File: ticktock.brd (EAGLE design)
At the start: 61 x 67.3 mm, 64 parts, among them IC1 ATMEGA644A, IC2 AD8611R, IC3 REF200U, J1 AVR_SPI_PRG_6NS, Q1 MOSFET-NCHANNEL2N7002PW, Q2 MOSFET-NCHANNELBSS138, Q3 MOSFET-NCHANNELBSS138, U1 MAX232SOIC16, U2 OSCILLATORSMD, U3 FT232RLSSOP, U4 BMP180

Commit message: Preliminary Route completed.
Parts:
- moved ATC4 2.03 mm to (19.8, 19.6), turned to 0 degrees
- moved GPR2 0.57 mm to (21.3, 8.64)
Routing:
- net GPS_TX: track 0.00 -> 122.0 mm, vias 0 -> 2
- net GPS_RX: track 0.00 -> 81.7 mm
- net 3.3V: track 28.5 -> 81.2 mm, vias 2 -> 6
- net 5V: track 291.8 -> 294.4 mm

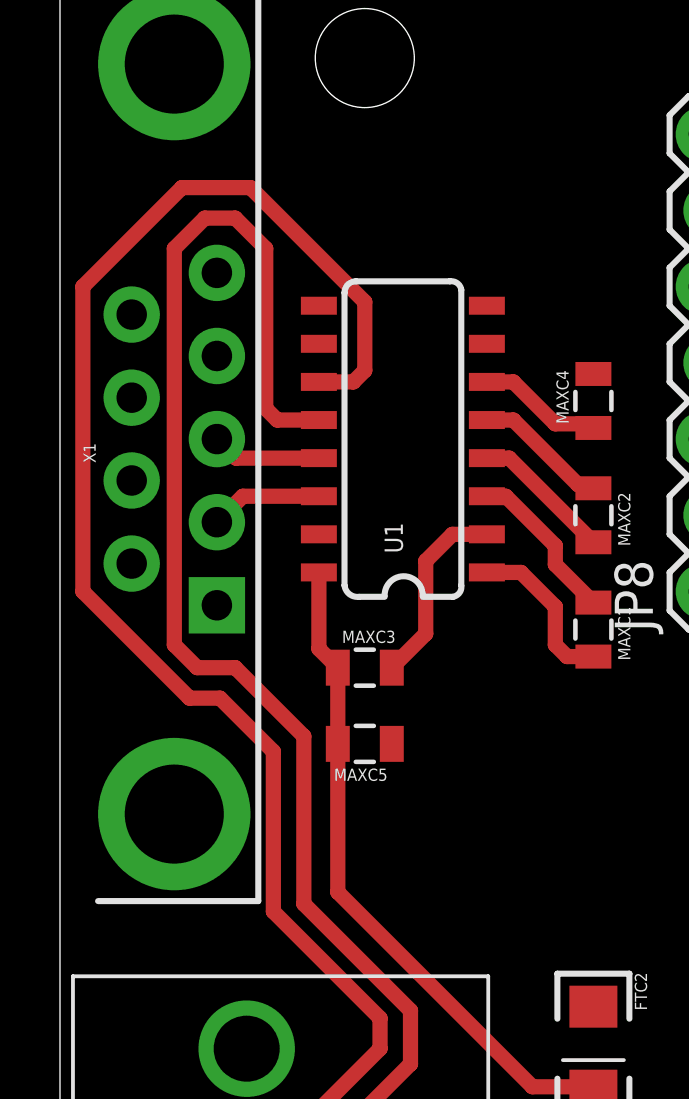
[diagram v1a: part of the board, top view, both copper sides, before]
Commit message: Fix traces around RS232 pins to use vias instead.
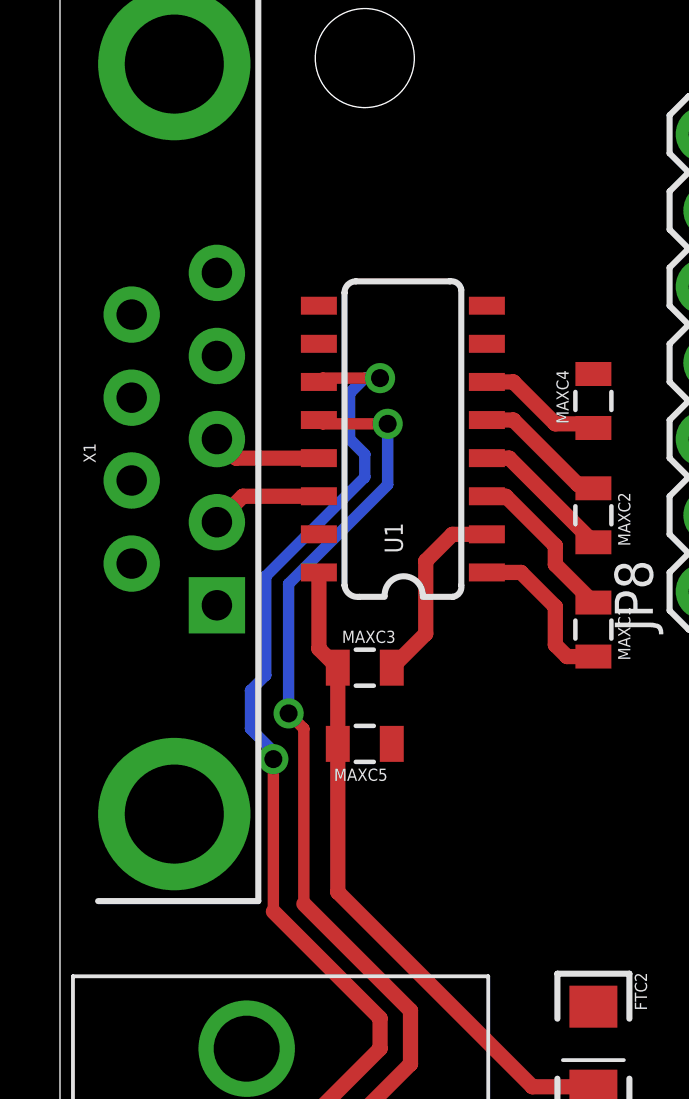
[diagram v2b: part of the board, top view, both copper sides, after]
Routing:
- net GPS_TX: track 122.0 -> 104.3 mm, vias 2 -> 4
- net GPS_RX: track 81.7 -> 66.1 mm, vias 0 -> 2
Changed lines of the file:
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@@
 <wire x1="33.824" y1="17.06" x2="33.02" y2="16.256" width="0.508" layer="1"/>
 <via x="33.02" y="16.256" extent="1-16" drill="0.6"/>
-<wire x1="8.63" y1="52.705" x2="9.779" y2="52.705" width="0.508" layer="1"/>
-<wire x1="9.779" y1="52.705" x2="10.16" y2="53.086" width="0.508" layer="1"/>
-<wire x1="10.16" y1="53.086" x2="10.16" y2="55.372" width="0.508" layer="1"/>
-<wire x1="10.16" y1="55.372" x2="6.35" y2="59.182" width="0.508" layer="1"/>
-<wire x1="6.35" y1="59.182" x2="4.064" y2="59.182" width="0.508" layer="1"/>
-<wire x1="4.064" y1="59.182" x2="0.762" y2="55.88" width="0.508" layer="1"/>
-<wire x1="0.762" y1="55.88" x2="0.762" y2="45.72" width="0.508" layer="1"/>
-<wire x1="0.762" y1="45.72" x2="4.318" y2="42.164" width="0.508" layer="1"/>
-<wire x1="4.318" y1="42.164" x2="5.334" y2="42.164" width="0.508" layer="1"/>
-<wire x1="5.334" y1="42.164" x2="7.112" y2="40.386" width="0.508" layer="1"/>
-<wire x1="7.112" y1="40.386" x2="7.112" y2="35.052" width="0.508" layer="1"/>
 <wire x1="7.112" y1="35.052" x2="10.668" y2="31.496" width="0.508" layer="1"/>
 <wire x1="10.668" y1="31.496" x2="10.668" y2="30.48" width="0.508" layer="1"/>
@@
 <wire x1="8.382" y1="10.16" x2="9.906" y2="11.684" width="0.381" layer="1"/>
 <wire x1="9.906" y1="11.684" x2="9.906" y2="20.066" width="0.381" layer="1"/>
+<wire x1="7.112" y1="35.052" x2="7.112" y2="40.132" width="0.381" layer="1"/>
+<via x="7.112" y="40.132" extent="1-16" drill="0.6"/>
+<wire x1="7.112" y1="40.132" x2="7.112" y2="40.386" width="0.381" layer="16"/>
+<wire x1="7.112" y1="40.386" x2="6.35" y2="41.148" width="0.381" layer="16"/>
+<wire x1="6.35" y1="41.148" x2="6.35" y2="42.418" width="0.381" layer="16"/>
+<wire x1="6.35" y1="42.418" x2="6.858" y2="42.926" width="0.381" layer="16"/>
+<wire x1="6.858" y1="42.926" x2="6.858" y2="46.228" width="0.381" layer="16"/>
+<wire x1="6.858" y1="46.228" x2="10.16" y2="49.53" width="0.381" layer="16"/>
+<wire x1="10.16" y1="49.53" x2="10.16" y2="50.292" width="0.381" layer="16"/>
+<wire x1="10.16" y1="50.292" x2="9.652" y2="50.8" width="0.381" layer="16"/>
+<wire x1="9.652" y1="50.8" x2="9.652" y2="52.324" width="0.381" layer="16"/>
+<wire x1="9.652" y1="52.324" x2="10.16" y2="52.832" width="0.381" layer="16"/>
+<wire x1="10.16" y1="52.832" x2="10.668" y2="52.832" width="0.381" layer="16"/>
+<via x="10.668" y="52.832" extent="1-16" drill="0.6"/>
+<wire x1="10.668" y1="52.832" x2="8.757" y2="52.832" width="0.381" layer="1"/>
+<wire x1="8.757" y1="52.832" x2="8.63" y2="52.705" width="0.381" layer="1"/>
 </signal>
 <signal name="N$8">
@@
 <wire x1="23.114" y1="15.748" x2="23.114" y2="19.558" width="0.508" layer="1"/>
 <wire x1="23.114" y1="19.558" x2="21.59" y2="21.082" width="0.508" layer="1"/>
-<wire x1="8.63" y1="51.435" x2="7.239" y2="51.435" width="0.508" layer="1"/>
-<wire x1="7.239" y1="51.435" x2="6.858" y2="51.816" width="0.508" layer="1"/>
-<wire x1="6.858" y1="51.816" x2="6.858" y2="57.15" width="0.508" layer="1"/>
-<wire x1="6.858" y1="57.15" x2="5.842" y2="58.166" width="0.508" layer="1"/>
-<wire x1="5.842" y1="58.166" x2="4.826" y2="58.166" width="0.508" layer="1"/>
-<wire x1="4.826" y1="58.166" x2="3.81" y2="57.15" width="0.508" layer="1"/>
-<wire x1="3.81" y1="57.15" x2="3.81" y2="43.942" width="0.508" layer="1"/>
-<wire x1="3.81" y1="43.942" x2="4.572" y2="43.18" width="0.508" layer="1"/>
-<wire x1="4.572" y1="43.18" x2="5.842" y2="43.18" width="0.508" layer="1"/>
-<wire x1="5.842" y1="43.18" x2="8.128" y2="40.894" width="0.508" layer="1"/>
-<wire x1="8.128" y1="40.894" x2="8.128" y2="35.306" width="0.508" layer="1"/>
 <wire x1="8.128" y1="35.306" x2="11.684" y2="31.75" width="0.508" layer="1"/>
 <wire x1="11.684" y1="31.75" x2="11.684" y2="29.972" width="0.508" layer="1"/>
@@
 <wire x1="8.636" y1="22.86" x2="10.414" y2="21.082" width="0.508" layer="1"/>
 <wire x1="10.414" y1="21.082" x2="21.59" y2="21.082" width="0.508" layer="1"/>
+<wire x1="8.128" y1="35.306" x2="8.128" y2="41.148" width="0.381" layer="1"/>
+<wire x1="8.128" y1="41.148" x2="7.62" y2="41.656" width="0.381" layer="1"/>
+<via x="7.62" y="41.656" extent="1-16" drill="0.6"/>
+<wire x1="7.62" y1="41.656" x2="7.62" y2="45.974" width="0.381" layer="16"/>
+<wire x1="7.62" y1="45.974" x2="10.922" y2="49.276" width="0.381" layer="16"/>
+<wire x1="10.922" y1="49.276" x2="10.922" y2="51.308" width="0.381" layer="16"/>
+<via x="10.922" y="51.308" extent="1-16" drill="0.6"/>
+<wire x1="10.922" y1="51.308" x2="8.757" y2="51.308" width="0.381" layer="1"/>
+<wire x1="8.757" y1="51.308" x2="8.63" y2="51.435" width="0.381" layer="1"/>
 </signal>
 <signal name="MISO">

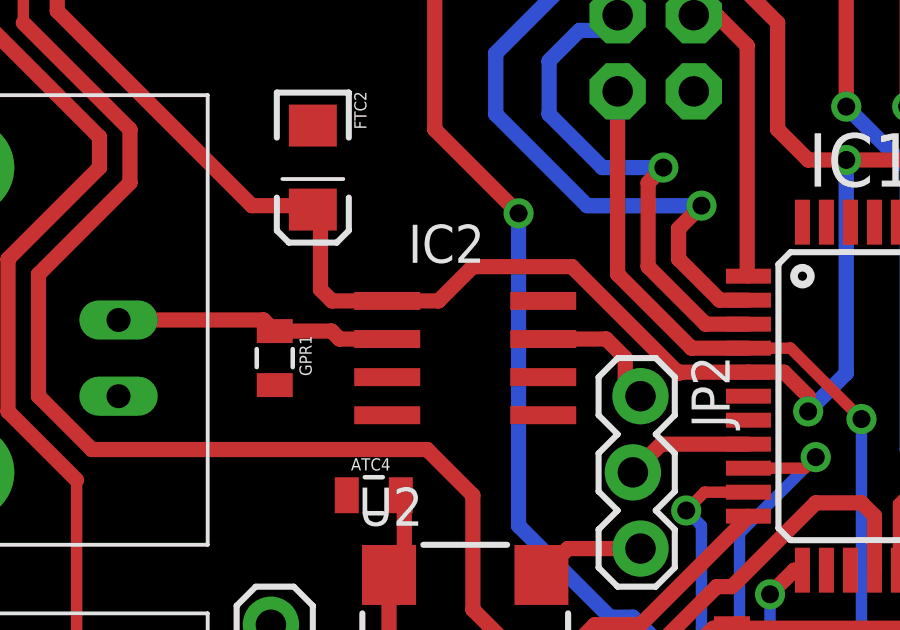
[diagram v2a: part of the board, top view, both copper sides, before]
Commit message: Replace SO8 package of ultrafast comparator with MSOP8 package.
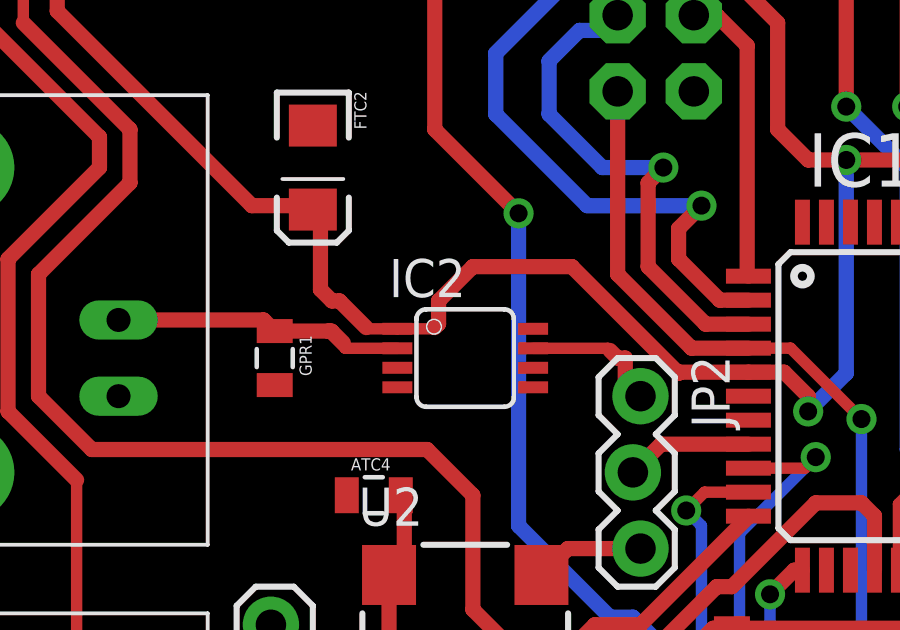
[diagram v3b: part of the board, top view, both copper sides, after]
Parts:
- IC2: value AD8611R -> AD8611RM; device analog-devices:SO8 -> analog-devices:MSOP08
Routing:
- net 5V: track 294.4 -> 295.6 mm
- net GPS_10MHZ: track 9.22 -> 10.4 mm
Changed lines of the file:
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@@
 <element name="ATC4" library="SparkFun-Capacitors" package="0805" value="0.01uF" x="19.812" y="19.558"/>
 <element name="JP2" library="SparkFun-Connectors" package="1X03_LOCK" value="" x="28.575" y="22.86" rot="R270"/>
-<element name="IC2" library="analog-devices" package="SO8" value="AD8611R" x="22.86" y="24.13" rot="R270"/>
+<element name="IC2" library="analog-devices" package="MSOP08" value="AD8611RM" x="22.86" y="24.13" rot="R270">
+<attribute name="OC_NEWARK" value="19M8930" x="22.86" y="24.13" size="1.778" layer="27" rot="R270" display="off"/>
+<attribute name="MPN" value="AD8611ARMZ-R2" x="22.86" y="24.13" size="1.778" layer="27" rot="R270" display="off"/>
+<attribute name="MF" value="" x="22.86" y="24.13" size="1.778" layer="27" rot="R270" display="off"/>
+<attribute name="OC_FARNELL" value="1464995" x="22.86" y="24.13" size="1.778" layer="27" rot="R270" display="off"/>
+</element>
 <element name="GPR1" library="SparkFun-Resistors" package="0805" value="50" x="16.51" y="24.13" rot="R270"/>
 <element name="GPR2" library="SparkFun-Resistors" package="0805" value="50" x="21.336" y="8.636"/>
@@
 <wire x1="38.1" y1="28.66" x2="43.9" y2="22.86" width="0" layer="19" extent="1-1"/>
 <wire x1="32.3" y1="22.86" x2="38.1" y2="28.66" width="0" layer="19" extent="1-1"/>
-<wire x1="25.46" y1="23.495" x2="32.3" y2="22.86" width="0" layer="19" extent="1-1"/>
-<wire x1="25.46" y1="22.225" x2="25.46" y2="23.495" width="0" layer="19" extent="1-1"/>
-<wire x1="20.26" y1="23.495" x2="25.46" y2="23.495" width="0" layer="19" extent="1-1"/>
-<wire x1="20.26" y1="22.225" x2="20.26" y2="23.495" width="0" layer="19" extent="1-1"/>
-<wire x1="18.912" y1="19.558" x2="20.26" y2="22.225" width="0" layer="19" extent="1-1"/>
-<wire x1="16.51" y1="23.23" x2="20.26" y2="23.495" width="0" layer="19" extent="1-1"/>
+<wire x1="25.122" y1="23.156" x2="32.3" y2="22.86" width="0" layer="19" extent="1-1"/>
+<wire x1="25.122" y1="23.806" x2="25.122" y2="23.156" width="0" layer="19" extent="1-1"/>
+<wire x1="20.597" y1="23.806" x2="25.122" y2="23.806" width="0" layer="19" extent="1-1"/>
+<wire x1="20.597" y1="23.156" x2="20.597" y2="23.806" width="0" layer="19" extent="1-1"/>
+<wire x1="18.912" y1="19.558" x2="20.597" y2="23.156" width="0" layer="19" extent="1-1"/>
+<wire x1="16.51" y1="23.23" x2="20.597" y2="23.156" width="0" layer="19" extent="1-1"/>
 <wire x1="11.303" y1="22.86" x2="16.51" y2="23.23" width="0" layer="19" extent="1-1"/>
-<wire x1="17.78" y1="31.88" x2="20.26" y2="23.495" width="0" layer="19" extent="1-1"/>
+<wire x1="17.78" y1="31.88" x2="20.597" y2="23.806" width="0" layer="19" extent="1-1"/>
 <wire x1="30.48" y1="33.02" x2="38.1" y2="28.66" width="0" layer="19" extent="1-1"/>
 <wire x1="25.4" y1="12.7" x2="18.912" y2="19.558" width="0" layer="19" extent="1-1"/>
@@
 <wire x1="18.034" y1="28.956" x2="18.034" y2="26.416" width="0.508" layer="1"/>
 <wire x1="18.034" y1="26.416" x2="18.415" y2="26.035" width="0.508" layer="1"/>
-<wire x1="20.26" y1="26.035" x2="18.415" y2="26.035" width="0.508" layer="1"/>
 <wire x1="49.16" y1="19.05" x2="51.816" y2="19.05" width="0.508" layer="1"/>
 <wire x1="51.816" y1="19.05" x2="52.324" y2="18.542" width="0.508" layer="1"/>
@@
 <wire x1="57.15" y1="38.55" x2="58.108" y2="38.55" width="0.508" layer="1"/>
 <wire x1="58.108" y1="38.55" x2="58.166" y2="38.608" width="0.508" layer="1"/>
-<wire x1="20.26" y1="26.035" x2="21.971" y2="26.035" width="0.508" layer="1"/>
 <wire x1="21.971" y1="26.035" x2="23.114" y2="27.178" width="0.508" layer="1"/>
 <wire x1="23.114" y1="27.178" x2="26.416" y2="27.178" width="0.508" layer="1"/>
@@
 <wire x1="29.505" y1="1.424" x2="29.505" y2="6.055" width="0.381" layer="1"/>
 <wire x1="29.505" y1="6.055" x2="29.464" y2="6.096" width="0.381" layer="1"/>
+<wire x1="18.415" y1="26.035" x2="18.669" y2="26.035" width="0.508" layer="1"/>
+<wire x1="18.669" y1="26.035" x2="19.558" y2="25.146" width="0.508" layer="1"/>
+<wire x1="21.971" y1="26.035" x2="21.971" y2="25.273" width="0.508" layer="1"/>
+<wire x1="21.971" y1="25.273" x2="21.844" y2="25.146" width="0.508" layer="1"/>
+<wire x1="20.597" y1="25.106" x2="19.598" y2="25.106" width="0.381" layer="1"/>
+<wire x1="19.598" y1="25.106" x2="19.558" y2="25.146" width="0.381" layer="1"/>
+<wire x1="20.597" y1="25.106" x2="21.804" y2="25.106" width="0.381" layer="1"/>
+<wire x1="21.804" y1="25.106" x2="21.844" y2="25.146" width="0.381" layer="1"/>
 </signal>
 <signal name="N$1">
@@
 <wire x1="11.303" y1="25.4" x2="16.14" y2="25.4" width="0.508" layer="1"/>
 <wire x1="16.14" y1="25.4" x2="16.51" y2="25.03" width="0.508" layer="1"/>
-<wire x1="16.51" y1="25.03" x2="18.404" y2="25.03" width="0.508" layer="1"/>
-<wire x1="18.404" y1="25.03" x2="18.669" y2="24.765" width="0.508" layer="1"/>
-<wire x1="20.26" y1="24.765" x2="18.669" y2="24.765" width="0.508" layer="1"/>
+<wire x1="16.51" y1="25.03" x2="18.288" y2="25.03" width="0.508" layer="1"/>
+<wire x1="18.288" y1="25.03" x2="18.404" y2="25.03" width="0.508" layer="1"/>
+<wire x1="18.404" y1="25.03" x2="18.796" y2="24.638" width="0.508" layer="1"/>
+<wire x1="20.597" y1="24.456" x2="18.862" y2="24.456" width="0.381" layer="1"/>
+<wire x1="18.862" y1="24.456" x2="18.288" y2="25.03" width="0.381" layer="1"/>
 </signal>
 <signal name="VCCIO">
@@
 <contactref element="JP2" pad="1"/>
 <contactref element="IC2" pad="7"/>
-<wire x1="25.46" y1="24.765" x2="27.559" y2="24.765" width="0.508" layer="1"/>
-<wire x1="27.559" y1="24.765" x2="28.194" y2="24.13" width="0.508" layer="1"/>
 <wire x1="28.702" y1="22.86" x2="28.194" y2="23.368" width="0.508" layer="1"/>
 <wire x1="28.194" y1="23.368" x2="28.194" y2="24.13" width="0.508" layer="1"/>
+<wire x1="28.194" y1="24.13" x2="27.94" y2="24.13" width="0.508" layer="1"/>
+<wire x1="27.94" y1="24.13" x2="27.686" y2="24.384" width="0.508" layer="1"/>
+<wire x1="25.122" y1="24.456" x2="27.614" y2="24.456" width="0.381" layer="1"/>
+<wire x1="27.614" y1="24.456" x2="27.686" y2="24.384" width="0.381" layer="1"/>
 </signal>
 <signal name="PD_CATHODE">
